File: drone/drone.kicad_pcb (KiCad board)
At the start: 2 copper layers, 50.8 x 50.8 mm, 43 parts, among them J1 Conn_01x06, J2 Conn_01x02, J3 Conn_01x02, J4 Conn_01x02, J5 Conn_01x02, J6 Conn_01x02, Q1 Si2319CDS, Q2 Si2319CDS, Q3 Si2319CDS, Q4 Si2319CDS, SW1 SW_Push_Open, SW2 SW_Push_Open, U1 ESP32-WROOM-32, U2 MPU-6050, U3 DWM1000, U4 BMP280, U5 TPS63001

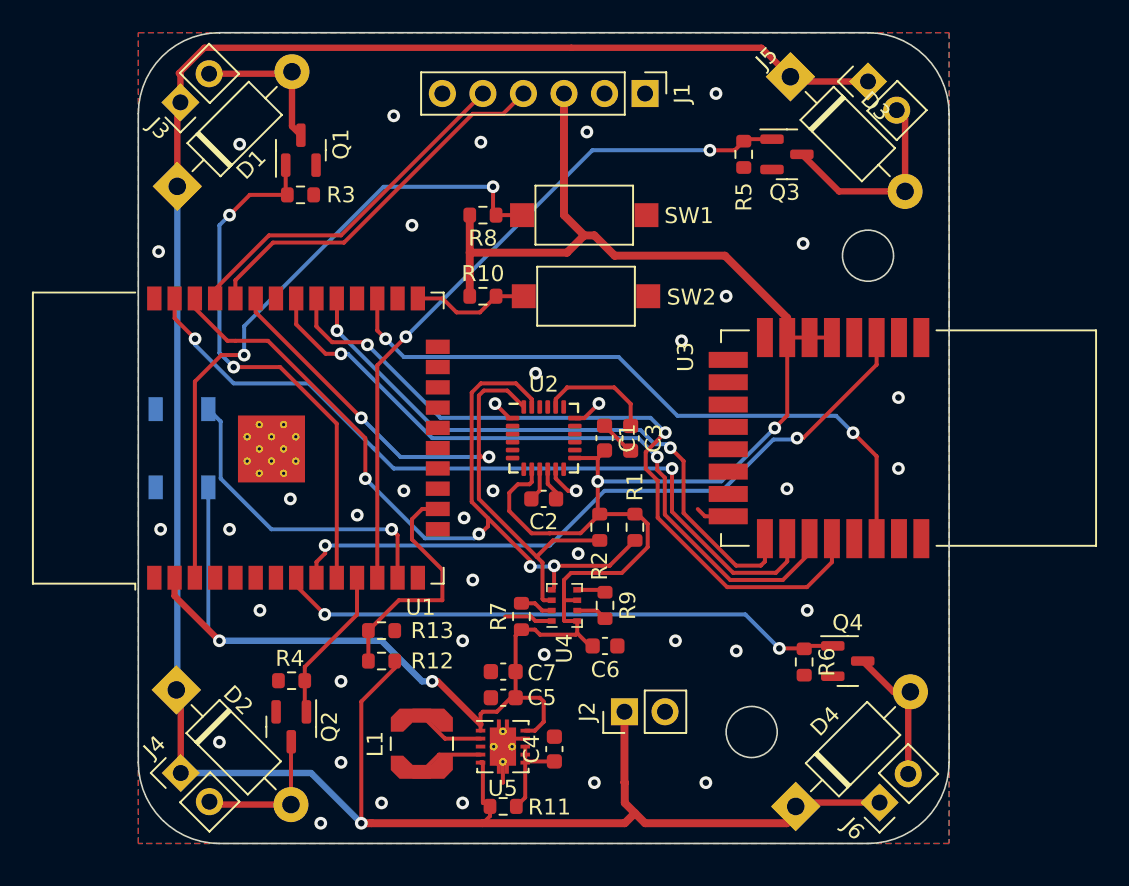
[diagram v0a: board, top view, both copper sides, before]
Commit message: add resistor current limitator
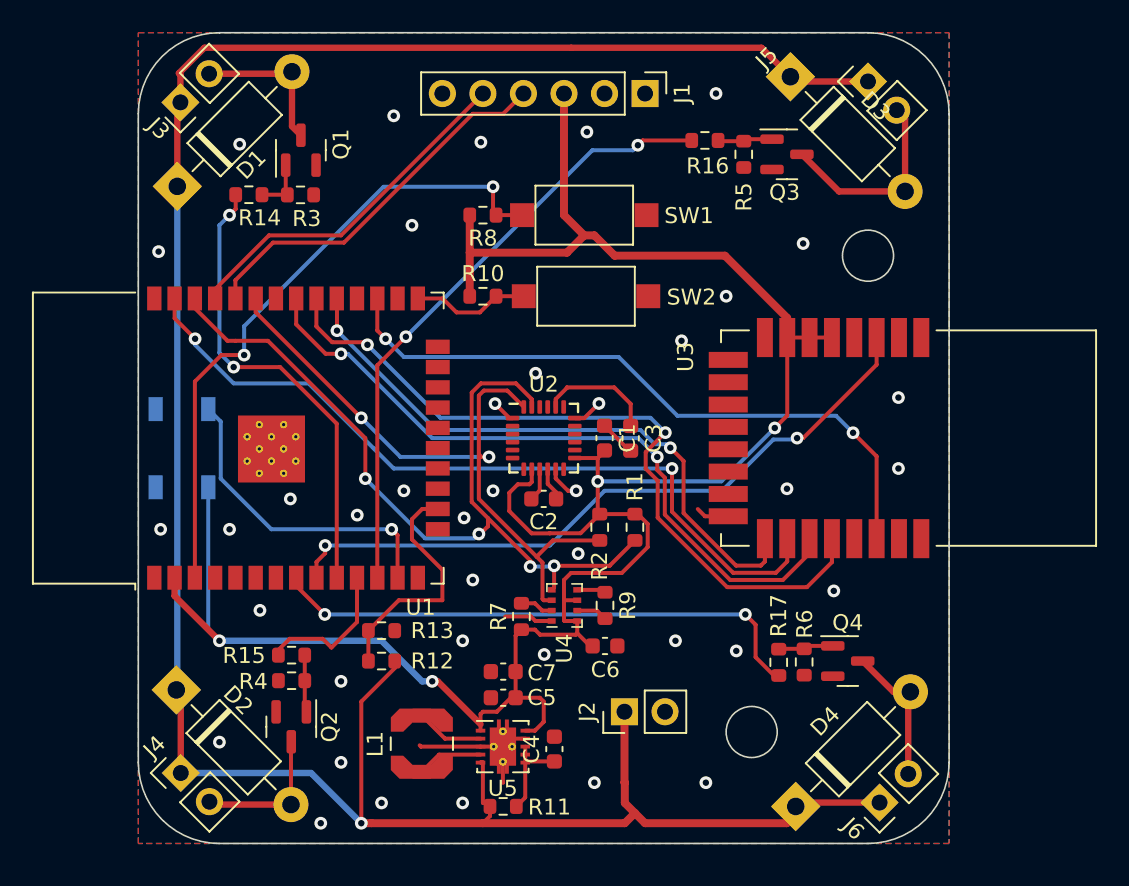
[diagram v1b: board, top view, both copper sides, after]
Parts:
- added R14: R_Small, Resistor_SMD:R_0603_1608Metric, F.Cu at (83.1, 86.3)
- added R15: R_Small, Resistor_SMD:R_0603_1608Metric, F.Cu at (85.8, 115.2)
- added R16: R_Small, Resistor_SMD:R_0603_1608Metric, F.Cu at (111.7, 83.0)
- added R17: R_Small, Resistor_SMD:R_0603_1608Metric, F.Cu at (116.3, 115.7)
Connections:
- Q1 pad 1: MOTOR_1 -> Net-(Q1-Pad1)
- Q2 pad 1: MOTOR_2 -> Net-(Q2-Pad1)
- Q3 pad 1: MOTOR_3 -> Net-(Q3-Pad1)
- Q4 pad 1: MOTOR_4 -> Net-(Q4-Pad1)
- R3 pad 1: MOTOR_1 -> Net-(Q1-Pad1)
- R4 pad 1: MOTOR_2 -> Net-(Q2-Pad1)
- R5 pad 1: MOTOR_3 -> Net-(Q3-Pad1)
- R6 pad 1: MOTOR_4 -> Net-(Q4-Pad1)
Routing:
- net MOTOR_3: track 43.9 -> 38.8 mm
- net GND: track 20.9 -> 25.5 mm
- net MOTOR_1: track 33.8 -> 29.2 mm
- net Net-(Q2-Pad1): track 0.00 -> 3.60 mm
- net Net-(Q4-Pad1): track 0.00 -> 3.51 mm
- net Net-(Q1-Pad1): track 0.00 -> 3.49 mm
- net Net-(Q3-Pad1): track 0.00 -> 3.45 mm
- net MOTOR_4: track 35.8 -> 34.3 mm
- net MOTOR_2: track 9.80 -> 9.21 mm

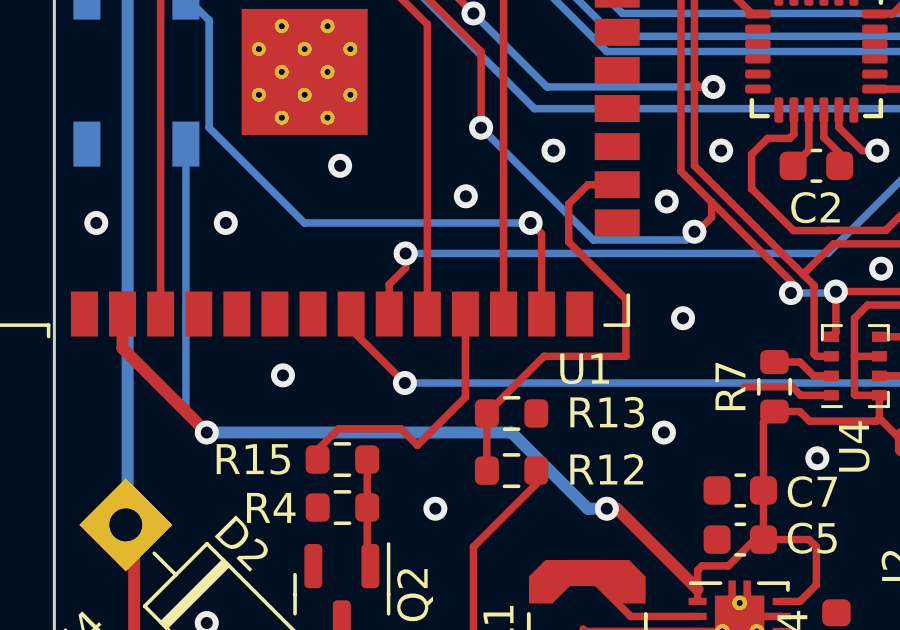
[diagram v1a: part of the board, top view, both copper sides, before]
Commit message: update adc bat level pin
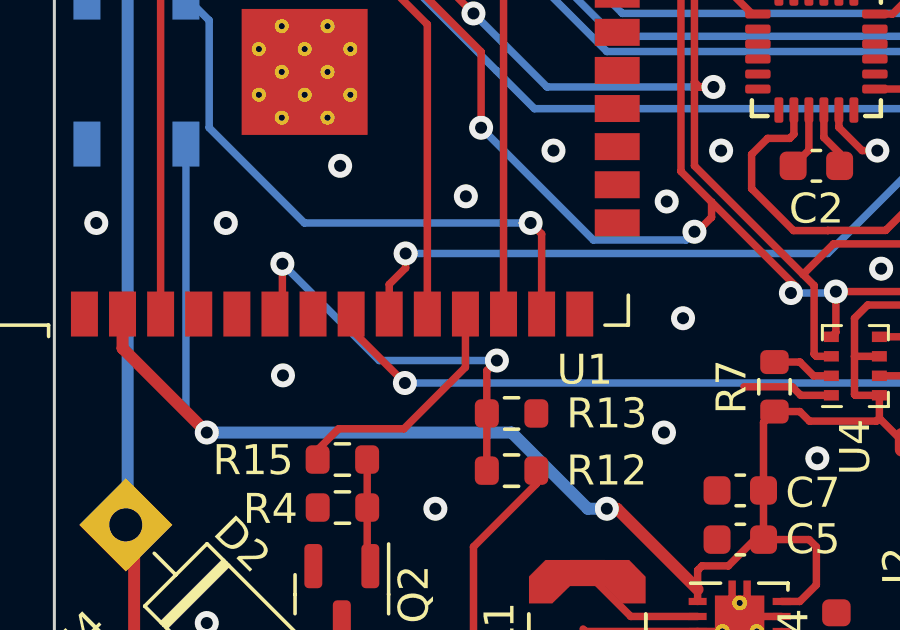
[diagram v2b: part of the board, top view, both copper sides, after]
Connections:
- U1 pad 16: BAT_LEVEL -> unconnected-(U1-Pad16)
- U1 pad 6: unconnected-(U1-Pad6) -> BAT_LEVEL
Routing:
- net MOTOR_2: track 9.21 -> 8.16 mm
- net BAT_LEVEL: track 15.1 -> 14.1 mm, vias 0 -> 2
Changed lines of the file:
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@@
   (net 31 "unconnected-(U1-Pad5)")
   (net 32 "unconnected-(U1-Pad17)")
-  (net 33 "unconnected-(U1-Pad6)")
+  (net 33 "unconnected-(U1-Pad16)")
   (net 34 "unconnected-(U1-Pad7)")
   (net 35 "GND")
@@
       (net 31 "unconnected-(U1-Pad5)") (pinfunction "SENSOR_VN") (pintype "input"))
     (pad "6" smd rect (at -8.75 -1.9 90) (size 1.5 0.9) (layers "F.Cu" "F.Paste" "F.Mask")
-      (net 33 "unconnected-(U1-Pad6)") (pinfunction "IO34") (pintype "input"))
+      (net 75 "BAT_LEVEL") (pinfunction "IO34") (pintype "input"))
     (pad "7" smd rect (at -8.75 -0.63 90) (size 1.5 0.9) (layers "F.Cu" "F.Paste" "F.Mask")
       (net 34 "unconnected-(U1-Pad7)") (pinfunction "IO35") (pintype "input"))
@@
       (net 35 "GND") (pinfunction "GND") (pintype "passive"))
     (pad "16" smd rect (at -4.44 9.51 180) (size 1.5 0.9) (layers "F.Cu" "F.Paste" "F.Mask")
-      (net 75 "BAT_LEVEL") (pinfunction "IO13") (pintype "bidirectional"))
+      (net 33 "unconnected-(U1-Pad16)") (pinfunction "IO13") (pintype "bidirectional"))
     (pad "17" smd rect (at -3.17 9.51 180) (size 1.5 0.9) (layers "F.Cu" "F.Paste" "F.Mask")
       (net 32 "unconnected-(U1-Pad17)") (pinfunction "SHD/SD2") (pintype "bidirectional"))
@@
   (segment (start 81.28 88.265) (end 81.28 96.257402) (width 0.25) (layer "B.Cu") (net 50))
   (segment (start 81.28 96.257402) (end 82.173299 97.150701) (width 0.25) (layer "B.Cu") (net 50))
-  (segment (start 87.75 114.175) (end 85.675 114.175) (width 0.25) (layer "F.Cu") (net 51))
-  (segment (start 88.3 114.725) (end 87.75 114.175) (width 0.25) (layer "F.Cu") (net 51))
+  (segment (start 89.902071 110.35) (end 89.902071 112.122929) (width 0.25) (layer "F.Cu") (net 51))
+  (segment (start 87.85 114.175) (end 85.675 114.175) (width 0.25) (layer "F.Cu") (net 51))
+  (segment (start 85.675 114.175) (end 84.975 114.875) (width 0.25) (layer "F.Cu") (net 51))
+  (segment (start 89.902071 112.122929) (end 87.85 114.175) (width 0.25) (layer "F.Cu") (net 51))
   (segment (start 84.975 114.875) (end 84.975 115.2) (width 0.25) (layer "F.Cu") (net 51))
-  (segment (start 85.675 114.175) (end 84.975 114.875) (width 0.25) (layer "F.Cu") (net 51))
-  (segment (start 89.902071 110.35) (end 89.902071 113.122929) (width 0.25) (layer "F.Cu") (net 51))
-  (segment (start 89.902071 113.122929) (end 88.3 114.725) (width 0.25) (layer "F.Cu") (net 51))
   (segment (start 91.172071 110.35) (end 91.172071 97.041929) (width 0.25) (layer "F.Cu") (net 52))
   (segment (start 91.172071 97.041929) (end 92.964 95.25) (width 0.25) (layer "F.Cu") (net 52))
@@
   (segment (start 81.359338 100.560248) (end 81.359338 104.14) (width 0.25) (layer "B.Cu") (net 74))
   (segment (start 80.584338 99.785248) (end 81.359338 100.560248) (width 0.25) (layer "B.Cu") (net 74))
-  (segment (start 90.615 113.665) (end 92.52 111.76) (width 0.25) (layer "F.Cu") (net 75))
-  (segment (start 92.52 111.76) (end 95.25 111.76) (width 0.25) (layer "F.Cu") (net 75))
-  (segment (start 93.345 107.95) (end 93.345 106.68) (width 0.25) (layer "F.Cu") (net 75))
-  (segment (start 95.25 111.76) (end 95.25 109.855) (width 0.25) (layer "F.Cu") (net 75))
-  (segment (start 95.25 109.855) (end 93.345 107.95) (width 0.25) (layer "F.Cu") (net 75))
+  (segment (start 90.615 113.665) (end 90.615 112.235) (width 0.25) (layer "F.Cu") (net 75))
+  (segment (start 90.615 112.235) (end 90.95 111.9) (width 0.25) (layer "F.Cu") (net 75))
+  (segment (start 83.8 108.675) (end 83.8 110.102071) (width 0.25) (layer "F.Cu") (net 75))
+  (segment (start 83.8 110.102071) (end 83.552071 110.35) (width 0.25) (layer "F.Cu") (net 75))
   (segment (start 90.615 113.665) (end 90.615 115.57) (width 0.25) (layer "F.Cu") (net 75))
-  (segment (start 93.985 106.04) (end 94.962071 106.04) (width 0.25) (layer "F.Cu") (net 75))
-  (segment (start 93.345 106.68) (end 93.985 106.04) (width 0.25) (layer "F.Cu") (net 75))
+  (via (at 90.95 111.9) (size 0.8) (drill 0.4) (layers "F.Cu" "B.Cu") (net 75))
+  (via (at 83.8 108.675) (size 0.8) (drill 0.4) (layers "F.Cu" "B.Cu") (net 75))
+  (segment (start 90.95 111.9) (end 87.025 111.9) (width 0.25) (layer "B.Cu") (net 75))
+  (segment (start 87.025 111.9) (end 83.8 108.675) (width 0.25) (layer "B.Cu") (net 75))
   (segment (start 85.434934 84.497496) (end 85.434934 86.259934) (width 0.25) (layer "F.Cu") (net 76))
   (segment (start 85.525 86.35) (end 85.535 86.36) (width 0.25) (layer "F.Cu") (net 76))
